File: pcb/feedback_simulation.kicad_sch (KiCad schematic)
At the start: 4 parts

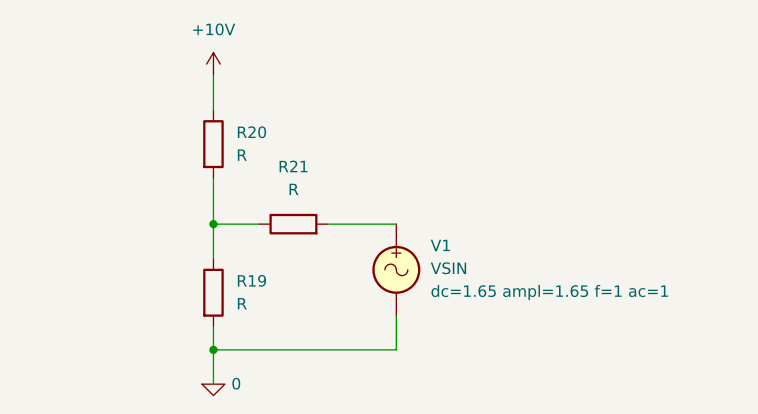
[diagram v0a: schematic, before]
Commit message: Added SMPlayer and Owrikbaars feedback simulation
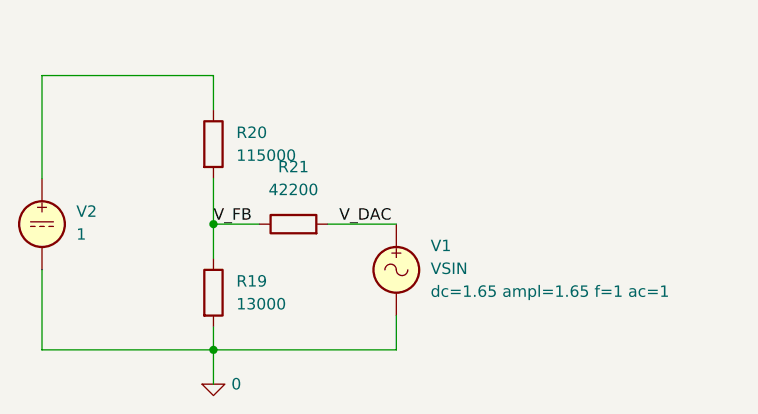
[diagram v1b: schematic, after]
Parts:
- added V2: 1, symbol Simulation_SPICE:VDC
- R19: value R -> 13000
- R20: value R -> 115000
- R21: value R -> 42200
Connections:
- net 0: now also V2.2
- net V_DAC: now reaches R21.2, V1.1
- net V_FB: now reaches R19.1, R20.2, R21.1
- net +10V: no longer names the net of R20.1
- net +10V: now also V2.1
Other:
- company: ${Author} -> Lea Calot
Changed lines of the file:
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@@
   (title_block
     (title "Feedback Resistor Network Simulation")
-    (company "${Author}")
-    (comment 1 "${Attribution}")
+    (company "Lea Calot")
   )
   (junction (at 134.62 92.71) (diameter 0) (color 0 0 0 0)
@@
   (junction (at 134.62 106.68) (diameter 0) (color 0 0 0 0)
   )
+  (wire (pts (xy 115.57 76.2) (xy 134.62 76.2))
+    (stroke (width 0) (type default))
+  )
   (wire (pts (xy 134.62 92.71) (xy 139.7 92.71))
     (stroke (width 0) (type default))
@@
     (stroke (width 0) (type default))
   )
+  (wire (pts (xy 115.57 106.68) (xy 134.62 106.68))
+    (stroke (width 0) (type default))
+  )
+  (wire (pts (xy 115.57 97.79) (xy 115.57 106.68))
+    (stroke (width 0) (type default))
+  )
+  (wire (pts (xy 115.57 87.63) (xy 115.57 76.2))
+    (stroke (width 0) (type default))
+  )
   (wire (pts (xy 134.62 104.14) (xy 134.62 106.68))
     (stroke (width 0) (type default))
+  )
+  (label "V_FB" (at 134.62 92.71 0) (fields_autoplaced)
+    (effects (font (size 1.27 1.27)) (justify left bottom))
+  )
+  (label "V_DAC" (at 148.59 92.71 0) (fields_autoplaced)
+    (effects (font (size 1.27 1.27)) (justify left bottom))
   )
   (symbol (lib_id "Simulation_SPICE:VSIN") (at 154.94 97.79 0) (unit 1)
@@
         )
       )
+      (project "feedback_simulation"
+        (path "/eeee3e5a-974c-4897-b8ae-c9353e8080b6"
+          (reference "V1") (unit 1)
+        )
+      )
     )
   )
@@
       (effects (font (size 1.27 1.27)) (justify left))
     )
-    (property "Value" "R" (at 137.16 85.09 0)
+    (property "Value" "115000" (at 137.16 85.09 0)
       (effects (font (size 1.27 1.27)) (justify left))
     )
@@
         )
       )
-    )
-  )
-  (symbol (lib_id "power:+10V") (at 134.62 76.2 0) (unit 1)
-    (in_bom yes) (on_board yes) (dnp no) (fields_autoplaced)
-    (property "Reference" "#PWR025" (at 134.62 80.01 0)
-      (effects (font (size 1.27 1.27)) hide)
-    )
-    (property "Value" "+10V" (at 134.62 71.12 0)
-      (effects (font (size 1.27 1.27)))
-    )
-    (property "Footprint" "" (at 134.62 76.2 0)
-      (effects (font (size 1.27 1.27)) hide)
-    )
-    (property "Datasheet" "" (at 134.62 76.2 0)
-      (effects (font (size 1.27 1.27)) hide)
-    )
-    (pin "1")
-    (instances
-      (project "shindensei"
-        (path "/958b377d-2cd7-45e0-91dd-b2d6e2ab8826/cd1c28ca-fcfa-4077-a49d-3272733b57f9"
-          (reference "#PWR025") (unit 1)
+      (project "feedback_simulation"
+        (path "/eeee3e5a-974c-4897-b8ae-c9353e8080b6"
+          (reference "R20") (unit 1)
         )
       )
@@
         )
       )
+      (project "feedback_simulation"
+        (path "/eeee3e5a-974c-4897-b8ae-c9353e8080b6"
+          (reference "#GND01") (unit 1)
+        )
+      )
+    )
+  )
+  (symbol (lib_id "Simulation_SPICE:VDC") (at 115.57 92.71 0) (unit 1)
+    (in_bom yes) (on_board yes) (dnp no) (fields_autoplaced)
+    (property "Reference" "V2" (at 119.38 91.3102 0)
+      (effects (font (size 1.27 1.27)) (justify left))
+    )
+    (property "Value" "1" (at 119.38 93.8502 0)
+      (effects (font (size 1.27 1.27)) (justify left))
+    )
+    (property "Footprint" "" (at 115.57 92.71 0)
+      (effects (font (size 1.27 1.27)) hide)
+    )
+    (property "Datasheet" "~" (at 115.57 92.71 0)
+      (effects (font (size 1.27 1.27)) hide)
+    )
+    (property "Sim.Pins" "1=+ 2=-" (at 115.57 92.71 0)
+      (effects (font (size 1.27 1.27)) hide)
+    )
+    (property "Sim.Type" "DC" (at 115.57 92.71 0)
+      (effects (font (size 1.27 1.27)) hide)
+    )
+    (property "Sim.Device" "V" (at 115.57 92.71 0)
+      (effects (font (size 1.27 1.27)) (justify left) hide)
+    )
+    (pin "1")
+    (pin "2")
+    (instances
+      (project "feedback_simulation"
+        (path "/eeee3e5a-974c-4897-b8ae-c9353e8080b6"
+          (reference "V2") (unit 1)
+        )
+      )
     )
   )
@@
       (effects (font (size 1.27 1.27)) (justify left))
     )
-    (property "Value" "R" (at 137.16 101.6 0)
+    (property "Value" "13000" (at 137.16 101.6 0)
       (effects (font (size 1.27 1.27)) (justify left))
     )
@@
       (project "shindensei"
         (path "/958b377d-2cd7-45e0-91dd-b2d6e2ab8826/cd1c28ca-fcfa-4077-a49d-3272733b57f9"
+          (reference "R19") (unit 1)
+        )
+      )
+      (project "feedback_simulation"
+        (path "/eeee3e5a-974c-4897-b8ae-c9353e8080b6"
           (reference "R19") (unit 1)
         )
@@
       (effects (font (size 1.27 1.27)))
     )
-    (property "Value" "R" (at 143.51 88.9 90)
+    (property "Value" "42200" (at 143.51 88.9 90)
       (effects (font (size 1.27 1.27)))
     )
@@
         )
       )
-    )
+      (project "feedback_simulation"
+        (path "/eeee3e5a-974c-4897-b8ae-c9353e8080b6"
+          (reference "R21") (unit 1)
+        )
+      )
+    )
+  )
+  (sheet_instances
+    (path "/" (page "1"))
   )
 )
